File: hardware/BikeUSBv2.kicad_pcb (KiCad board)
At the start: 2 copper layers, 43.6 x 25.5 mm, 53 parts, among them J1 TYPE-C-31-M-16, J2 JST S2B-EH(LF)(SN), SW1 1TS002E-2500-2501-CT, SW2 1TS002E-2500-2501-CT, U1 TPS63070, U2 ATtiny1616-M, U3 FUSB302B10MPX, U4 HT7550

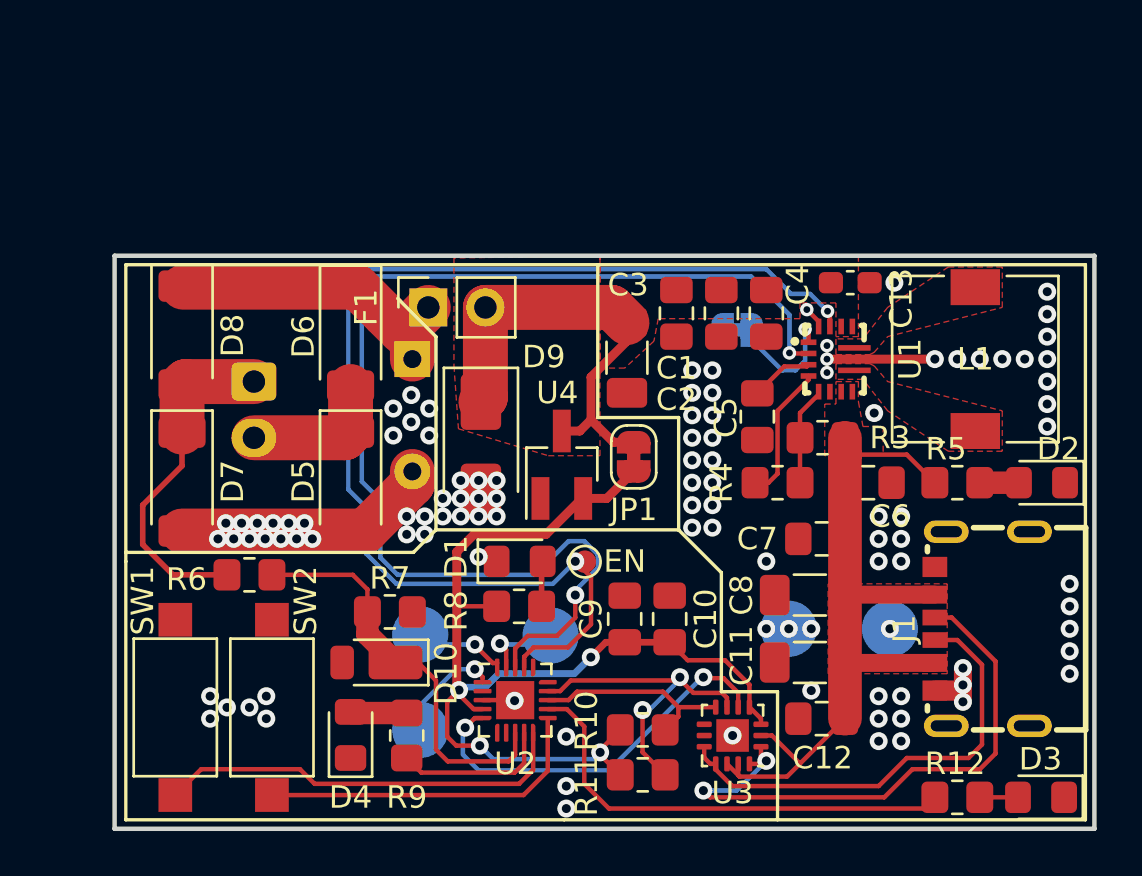
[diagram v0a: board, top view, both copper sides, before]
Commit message: [PCB] different Zener
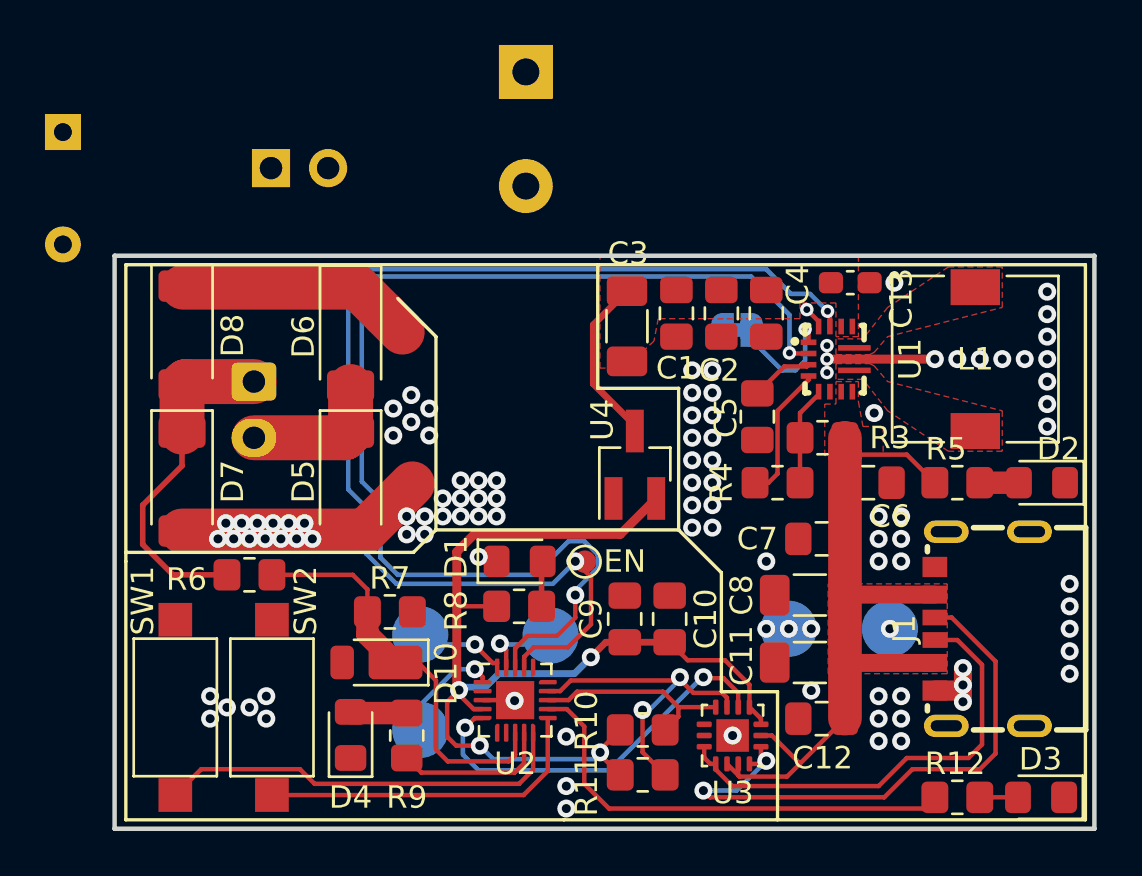
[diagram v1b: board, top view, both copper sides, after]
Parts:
- removed JP1: SolderJumper_2_Bridged, Jumper:SolderJumper-2_P1.3mm_Bridged_RoundedPad1.0x1.5mm
- D9: value 18V -> 1N5353B; footprint Diode_SMD:D_SMA -> Diode_THT:D_DO-27_P5.08mm_Vertical_AnodeUp; moved to B.Cu
- F1: value 3A -> 60°C; moved to B.Cu
- moved C0 18.5 mm to (107.7, 76.9)
- moved D9 16.8 mm to (128.3, 74.2)
- moved F1 9.35 mm to (117.0, 78.5), turned to -90 degrees
- moved U4 3.25 mm to (133.2, 91.7)
- moved C3 1.40 mm to (132.8, 85.5)
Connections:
- C0 pad 1: VPP -> +6V
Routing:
- net +6V: track 19.7 -> 7.61 mm
- net VPP: track 13.2 -> 10.6 mm
- net GND: track 27.5 -> 26.9 mm
- net VCC: track 47.8 -> 48.3 mm

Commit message: [PCB] switch to different protection circuit
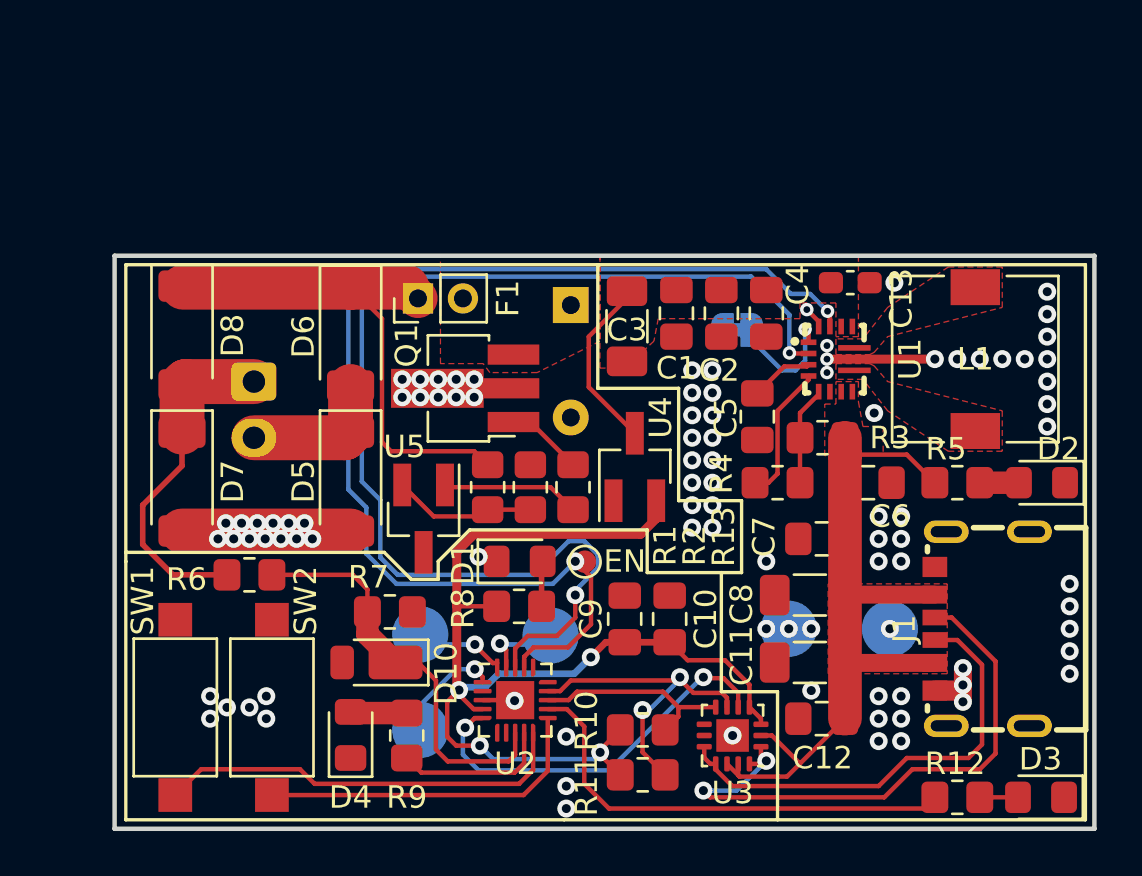
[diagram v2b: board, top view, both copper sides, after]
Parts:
- removed D9: 1N5353B, Diode_THT:D_DO-27_P5.08mm_Vertical_AnodeUp
- added Q1: 2SB772SQ, Package_TO_SOT_SMD:SOT-89-3_Handsoldering, F.Cu at (125.3, 88.3)
- added R1: 130k, Resistor_SMD:R_0805_2012Metric_Pad1.20x1.40mm_HandSolder, F.Cu at (126.6, 92.7)
- added R13: 1k, Resistor_SMD:R_0805_2012Metric_Pad1.20x1.40mm_HandSolder, F.Cu at (130.4, 92.7)
- added R2: 24k, Resistor_SMD:R_0805_2012Metric_Pad1.20x1.40mm_HandSolder, F.Cu at (128.5, 92.7)
- added U5: TL431AIDBZR, Package_TO_SOT_SMD:SOT-23_Handsoldering, F.Cu at (123.8, 94.1)
- F1: footprint Connector_PinSocket_2.54mm:PinSocket_1x02_P2.54mm_Vertical -> Connector_PinHeader_2.00mm:PinHeader_1x02_P2.00mm_Vertical; moved to F.Cu
- moved C0 23.9 mm to (130.3, 84.6)
- moved F1 8.74 mm to (123.5, 84.3), turned to 90 degrees
- moved U4 0.10 mm to (133.2, 91.8)
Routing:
- net VPP: track 10.6 -> 23.3 mm
- net Net-(U5-REF): track 0.00 -> 6.40 mm
- net Net-(U5-K): track 0.00 -> 6.16 mm
- net GND: track 26.9 -> 23.3 mm, vias 105 -> 94
- net Net-(Q1-B): track 0.00 -> 3.44 mm
- net VCC: track 48.3 -> 48.8 mm

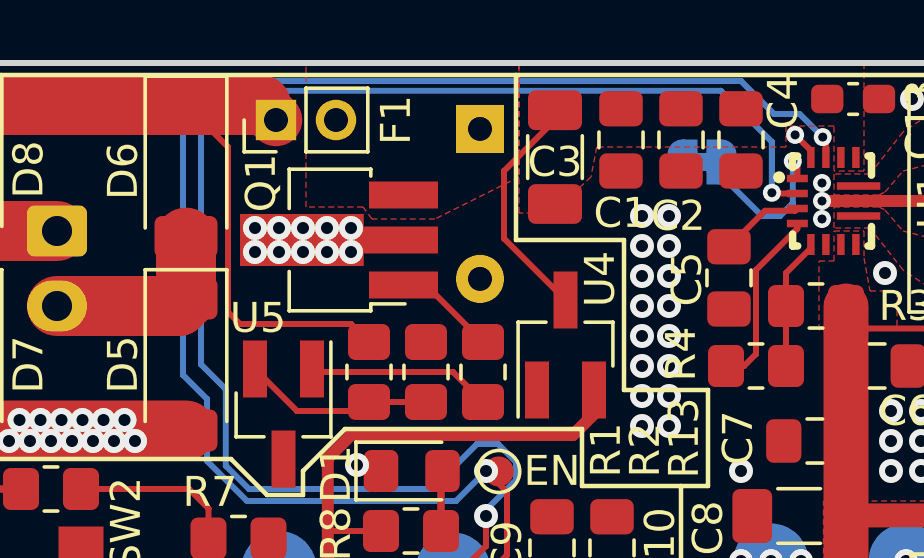
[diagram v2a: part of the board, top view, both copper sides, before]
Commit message: [PCB] fix DRC
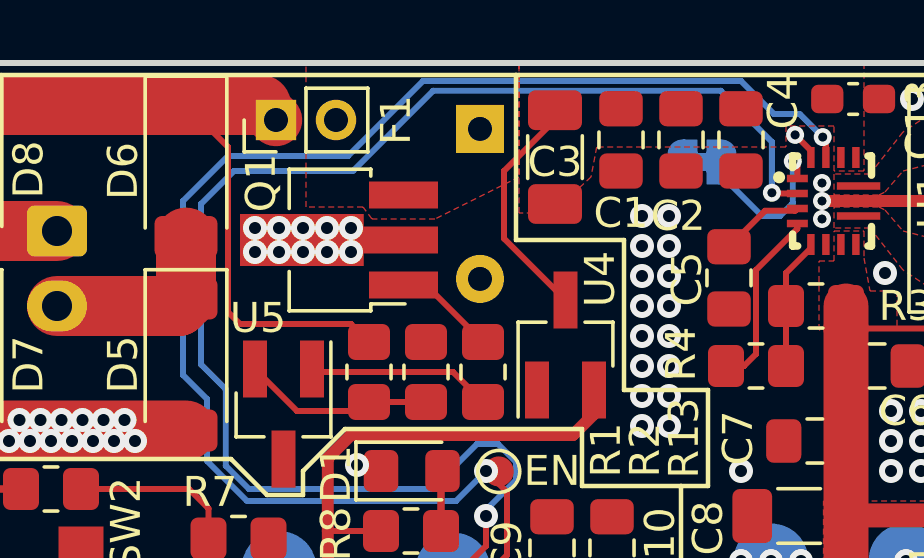
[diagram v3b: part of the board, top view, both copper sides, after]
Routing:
- net /EN: track 52.9 -> 50.9 mm
- net /PG: track 52.9 -> 51.1 mm
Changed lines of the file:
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@@
   (via (at 141.724777 84.869661) (size 0.6) (drill 0.3) (layers "F.Cu" "B.Cu") (net 17))
   (via (at 130.5 96) (size 0.8) (drill 0.4) (layers "F.Cu" "B.Cu") (net 17))
+  (segment (start 125.9 85.5) (end 121.9 85.5) (width 0.2) (layer "B.Cu") (net 17))
+  (segment (start 120.4 87) (end 120.4 92.8) (width 0.2) (layer "B.Cu") (net 17))
+  (segment (start 141.724777 84.869661) (end 140.955116 84.1) (width 0.2) (layer "B.Cu") (net 17))
+  (segment (start 140.098529 84.1) (end 138.998529 83) (width 0.2) (layer "B.Cu") (net 17))
+  (segment (start 140.955116 84.1) (end 140.098529 84.1) (width 0.2) (layer "B.Cu") (net 17))
+  (segment (start 121.2 95.662448) (end 122.537552 97) (width 0.2) (layer "B.Cu") (net 17))
+  (segment (start 121.2 93.6) (end 121.2 95.662448) (width 0.2) (layer "B.Cu") (net 17))
+  (segment (start 120.4 92.8) (end 121.2 93.6) (width 0.2) (layer "B.Cu") (net 17))
+  (segment (start 128.4 83) (end 125.9 85.5) (width 0.2) (layer "B.Cu") (net 17))
+  (segment (start 121.9 85.5) (end 120.4 87) (width 0.2) (layer "B.Cu") (net 17))
   (segment (start 129.5 97) (end 130.5 96) (width 0.2) (layer "B.Cu") (net 17))
-  (segment (start 121 83) (end 120.4 83.6) (width 0.2) (layer "B.Cu") (net 17))
-  (segment (start 120.4 92.8) (end 121.2 93.6) (width 0.2) (layer "B.Cu") (net 17))
-  (segment (start 140.098529 84.1) (end 138.998529 83) (width 0.2) (layer "B.Cu") (net 17))
-  (segment (start 120.4 83.6) (end 120.4 92.8) (width 0.2) (layer "B.Cu") (net 17))
-  (segment (start 141.724777 84.869661) (end 140.955116 84.1) (width 0.2) (layer "B.Cu") (net 17))
-  (segment (start 138.998529 83) (end 121 83) (width 0.2) (layer "B.Cu") (net 17))
-  (segment (start 121.2 93.6) (end 121.2 95.662448) (width 0.2) (layer "B.Cu") (net 17))
   (segment (start 122.537552 97) (end 129.5 97) (width 0.2) (layer "B.Cu") (net 17))
-  (segment (start 121.2 95.662448) (end 122.537552 97) (width 0.2) (layer "B.Cu") (net 17))
-  (segment (start 140.955116 84.1) (end 140.098529 84.1) (width 0.2) (layer "B.Cu") (net 17))
+  (segment (start 138.998529 83) (end 128.4 83) (width 0.2) (layer "B.Cu") (net 17))
   (segment (start 140.029215 86.725727) (end 140.053488 86.75) (width 0.2) (layer "F.Cu") (net 18))
   (segment (start 140.053488 86.75) (end 140.88 86.75) (width 0.2) (layer "F.Cu") (net 18))
@@
   (via (at 140.029215 86.725727) (size 0.6) (drill 0.3) (layers "F.Cu" "B.Cu") (net 18))
   (via (at 130.5 97.5) (size 0.8) (drill 0.4) (layers "F.Cu" "B.Cu") (net 18))
-  (segment (start 121 83.962448) (end 121 92.447602) (width 0.2) (layer "B.Cu") (net 18))
+  (segment (start 122.6 96.6) (end 128.7 96.6) (width 0.2) (layer "B.Cu") (net 18))
+  (segment (start 131.5 96.3) (end 130.5 97.3) (width 0.2) (layer "B.Cu") (net 18))
+  (segment (start 138.327 83.327) (end 128.735448 83.327) (width 0.2) (layer "B.Cu") (net 18))
+  (segment (start 121.827 95.827) (end 122.6 96.6) (width 0.2) (layer "B.Cu") (net 18))
+  (segment (start 121 92.447602) (end 121.827 93.274602) (width 0.2) (layer "B.Cu") (net 18))
+  (segment (start 128.735448 83.327) (end 126.062448 86) (width 0.2) (layer "B.Cu") (net 18))
+  (segment (start 130.2 95.1) (end 130.9 95.1) (width 0.2) (layer "B.Cu") (net 18))
+  (segment (start 128.7 96.6) (end 130.2 95.1) (width 0.2) (layer "B.Cu") (net 18))
   (segment (start 121.827 93.274602) (end 121.827 95.827) (width 0.2) (layer "B.Cu") (net 18))
-  (segment (start 138.327 83.327) (end 121.635448 83.327) (width 0.2) (layer "B.Cu") (net 18))
+  (segment (start 121 87.1) (end 121 92.447602) (width 0.2) (layer "B.Cu") (net 18))
+  (segment (start 126.062448 86) (end 122.1 86) (width 0.2) (layer "B.Cu") (net 18))
+  (segment (start 140.029215 85.029215) (end 138.327 83.327) (width 0.2) (layer "B.Cu") (net 18))
+  (segment (start 130.5 97.3) (end 130.5 97.5) (width 0.2) (layer "B.Cu") (net 18))
+  (segment (start 140.029215 86.725727) (end 140.029215 85.029215) (width 0.2) (layer "B.Cu") (net 18))
   (segment (start 130.9 95.1) (end 131.5 95.7) (width 0.2) (layer "B.Cu") (net 18))
   (segment (start 131.5 95.7) (end 131.5 96.3) (width 0.2) (layer "B.Cu") (net 18))
-  (segment (start 121.635448 83.327) (end 121 83.962448) (width 0.2) (layer "B.Cu") (net 18))
-  (segment (start 121 92.447602) (end 121.827 93.274602) (width 0.2) (layer "B.Cu") (net 18))
-  (segment (start 122.6 96.6) (end 128.7 96.6) (width 0.2) (layer "B.Cu") (net 18))
-  (segment (start 140.029215 86.725727) (end 140.029215 85.029215) (width 0.2) (layer "B.Cu") (net 18))
-  (segment (start 140.029215 85.029215) (end 138.327 83.327) (width 0.2) (layer "B.Cu") (net 18))
-  (segment (start 130.5 97.3) (end 130.5 97.5) (width 0.2) (layer "B.Cu") (net 18))
-  (segment (start 130.2 95.1) (end 130.9 95.1) (width 0.2) (layer "B.Cu") (net 18))
-  (segment (start 121.827 95.827) (end 122.6 96.6) (width 0.2) (layer "B.Cu") (net 18))
-  (segment (start 131.5 96.3) (end 130.5 97.3) (width 0.2) (layer "B.Cu") (net 18))
-  (segment (start 128.7 96.6) (end 130.2 95.1) (width 0.2) (layer "B.Cu") (net 18))
+  (segment (start 122.1 86) (end 121 87.1) (width 0.2) (layer "B.Cu") (net 18))
   (segment (start 128.225 104.975) (end 128.225 103.625) (width 0.2) (layer "F.Cu") (net 19))
   (segment (start 127.8 105.4) (end 128.225 104.975) (width 0.2) (layer "F.Cu") (net 19))

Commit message: [PCB] fill in LCSC IDs
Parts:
- F1: value 60°C -> 76°C; footprint Connector_PinHeader_2.00mm:PinHeader_1x02_P2.00mm_Vertical -> Connector_PinSocket_2.54mm:PinSocket_1x02_P2.54mm_Vertical
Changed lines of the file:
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@@
     (descr "SOT-89-3 Handsoldering")
     (tags "SOT-89-3 Handsoldering")
+    (property "LCSC" "C5158798")
     (property "Sheetfile" "BikeUSBv2.kicad_sch")
     (property "Sheetname" "")
@@
     (descr "SOT-23, Handsoldering")
     (tags "SOT-23")
+    (property "LCSC" "C23892")
     (property "Sheetfile" "BikeUSBv2.kicad_sch")
     (property "Sheetname" "")
@@
     )
   )
-  (footprint "Connector_PinHeader_2.00mm:PinHeader_1x02_P2.00mm_Vertical" (layer "F.Cu")
+  (footprint "Connector_PinSocket_2.54mm:PinSocket_1x02_P2.54mm_Vertical" (layer "F.Cu")
     (at 123.5 84.3 90)
-    (descr "Through hole straight pin header, 1x02, 2.00mm pitch, single row")
-    (tags "Through hole pin header THT 1x02 2.00mm single row")
+    (descr "Through hole straight socket strip, 1x02, 2.54mm pitch, single row (from Kicad 4.0.7), script generated")
+    (tags "Through hole socket strip THT 1x02 2.54mm single row")
+    (property "LCSC" "C22396315")
+    (property "Manufacturer" "SETsafe | SETfuse")
+    (property "Part #" "X0")
     (property "Sheetfile" "BikeUSBv2.kicad_sch")
     (property "Sheetname" "")
@@
     (property "ki_keywords" "temperature switch")
     (attr through_hole)
-    (fp_text reference "F1" (at 0 4 90) (layer "F.SilkS")
-        (effects (font (size 1 1) (thickness 0.15)))
-    )
-    (fp_text value "60°C" (at 0 4.06 90) (layer "F.Fab")
-        (effects (font (size 1 1) (thickness 0.15)))
-    )
-    (fp_text user "${REFERENCE}" (at 0 1) (layer "F.Fab")
-        (effects (font (size 1 1) (thickness 0.15)))
-    )
-    (fp_line (start -1.06 -1.06) (end 0 -1.06)
-      (stroke (width 0.12) (type solid)) (layer "F.SilkS"))
-    (fp_line (start -1.06 0) (end -1.06 -1.06)
-      (stroke (width 0.12) (type solid)) (layer "F.SilkS"))
-    (fp_line (start -1.06 1) (end -1.06 3.06)
-      (stroke (width 0.12) (type solid)) (layer "F.SilkS"))
-    (fp_line (start -1.06 1) (end 1.06 1)
-      (stroke (width 0.12) (type solid)) (layer "F.SilkS"))
-    (fp_line (start -1.06 3.06) (end 1.06 3.06)
-      (stroke (width 0.12) (type solid)) (layer "F.SilkS"))
-    (fp_line (start 1.06 1) (end 1.06 3.06)
-      (stroke (width 0.12) (type solid)) (layer "F.SilkS"))
-    (fp_line (start -1.5 -1.5) (end -1.5 3.5)
-      (stroke (width 0.05) (type solid)) (layer "F.CrtYd"))
-    (fp_line (start -1.5 3.5) (end 1.5 3.5)
-      (stroke (width 0.05) (type solid)) (layer "F.CrtYd"))
-    (fp_line (start 1.5 -1.5) (end -1.5 -1.5)
-      (stroke (width 0.05) (type solid)) (layer "F.CrtYd"))
-    (fp_line (start 1.5 3.5) (end 1.5 -1.5)
-      (stroke (width 0.05) (type solid)) (layer "F.CrtYd"))
-    (fp_line (start -1 -0.5) (end -0.5 -1)
-      (stroke (width 0.1) (type solid)) (layer "F.Fab"))
-    (fp_line (start -1 3) (end -1 -0.5)
-      (stroke (width 0.1) (type solid)) (layer "F.Fab"))
-    (fp_line (start -0.5 -1) (end 1 -1)
-      (stroke (width 0.1) (type solid)) (layer "F.Fab"))
-    (fp_line (start 1 -1) (end 1 3)
-      (stroke (width 0.1) (type solid)) (layer "F.Fab"))
-    (fp_line (start 1 3) (end -1 3)
-      (stroke (width 0.1) (type solid)) (layer "F.Fab"))
-    (pad "1" thru_hole rect (at 0 0 90) (size 1.35 1.35) (drill 0.8) (layers "*.Cu" "*.Mask")
+    (fp_text reference "F1" (at 0 -2.77 90) (layer "F.SilkS")
+        (effects (font (size 1 1) (thickness 0.15)))
+    )
+    (fp_text value "76°C" (at 0 5.31 90) (layer "F.Fab")
+        (effects (font (size 1 1) (thickness 0.15)))
+    )
+    (fp_text user "${REFERENCE}" (at 0 1.27 180) (layer "F.Fab")
+        (effects (font (size 1 1) (thickness 0.15)))
+    )
+    (fp_line (start -1.33 1.27) (end -1.33 3.87)
+      (stroke (width 0.12) (type solid)) (layer "F.SilkS"))
+    (fp_line (start -1.33 1.27) (end 1.33 1.27)
+      (stroke (width 0.12) (type solid)) (layer "F.SilkS"))
+    (fp_line (start -1.33 3.87) (end 1.33 3.87)
+      (stroke (width 0.12) (type solid)) (layer "F.SilkS"))
+    (fp_line (start 0 -1.33) (end 1.33 -1.33)
+      (stroke (width 0.12) (type solid)) (layer "F.SilkS"))
+    (fp_line (start 1.33 -1.33) (end 1.33 0)
+      (stroke (width 0.12) (type solid)) (layer "F.SilkS"))
+    (fp_line (start 1.33 1.27) (end 1.33 3.87)
+      (stroke (width 0.12) (type solid)) (layer "F.SilkS"))
+    (fp_line (start -1.8 -1.8) (end 1.75 -1.8)
+      (stroke (width 0.05) (type solid)) (layer "F.CrtYd"))
+    (fp_line (start -1.8 4.3) (end -1.8 -1.8)
+      (stroke (width 0.05) (type solid)) (layer "F.CrtYd"))
+    (fp_line (start 1.75 -1.8) (end 1.75 4.3)
+      (stroke (width 0.05) (type solid)) (layer "F.CrtYd"))
+    (fp_line (start 1.75 4.3) (end -1.8 4.3)
+      (stroke (width 0.05) (type solid)) (layer "F.CrtYd"))
+    (fp_line (start -1.27 -1.27) (end 0.635 -1.27)
+      (stroke (width 0.1) (type solid)) (layer "F.Fab"))
+    (fp_line (start -1.27 3.81) (end -1.27 -1.27)
+      (stroke (width 0.1) (type solid)) (layer "F.Fab"))
+    (fp_line (start 0.635 -1.27) (end 1.27 -0.635)
+      (stroke (width 0.1) (type solid)) (layer "F.Fab"))
+    (fp_line (start 1.27 -0.635) (end 1.27 3.81)
+      (stroke (width 0.1) (type solid)) (layer "F.Fab"))
+    (fp_line (start 1.27 3.81) (end -1.27 3.81)
+      (stroke (width 0.1) (type solid)) (layer "F.Fab"))
+    (pad "1" thru_hole rect (at 0 0 90) (size 1.7 1.7) (drill 1) (layers "*.Cu" "*.Mask")
       (net 31 "VPP") (pinfunction "A") (pintype "passive"))
-    (pad "2" thru_hole oval (at 0 2 90) (size 1.35 1.35) (drill 0.8) (layers "*.Cu" "*.Mask")
+    (pad "2" thru_hole oval (at 0 2.54 90) (size 1.7 1.7) (drill 1) (layers "*.Cu" "*.Mask")
       (net 32 "+6V") (pinfunction "B") (pintype "passive"))
-    (model "${KICAD6_3DMODEL_DIR}/Connector_PinHeader_2.00mm.3dshapes/PinHeader_1x02_P2.00mm_Vertical.wrl"
-      (offset (xyz 0 0 0))
-      (scale (xyz 1 1 1))
+    (model "${KICAD6_3DMODEL_DIR}/Connector_PinSocket_2.54mm.3dshapes/PinSocket_1x02_P2.54mm_Vertical.wrl"
+      (offset (xyz 0 0 0))
+      (scale (xyz 1 1 1))
